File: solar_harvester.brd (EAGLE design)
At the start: 46 x 25.4 mm, 35 parts, among them U1 BQ25505, U2 TPS61322XA, U3 TPS61322XA, U4 MAX17040, U5 INA226

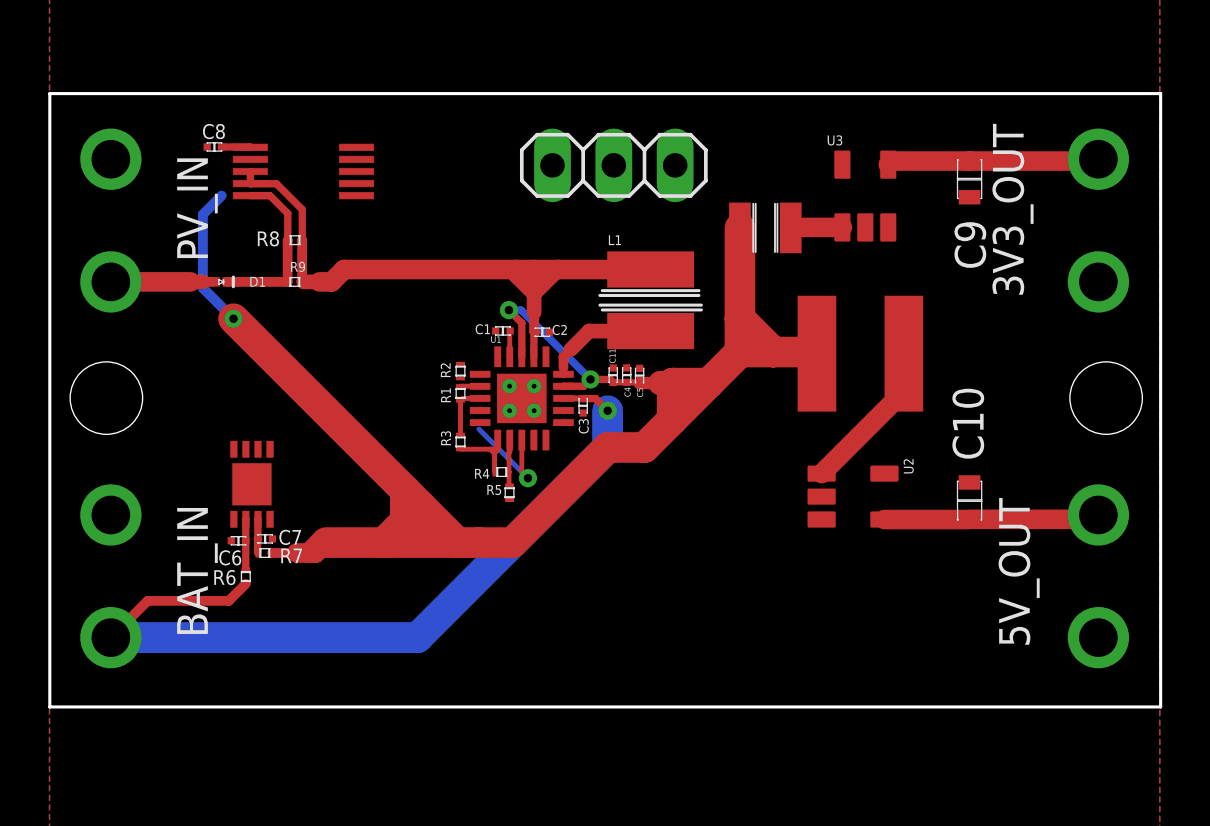
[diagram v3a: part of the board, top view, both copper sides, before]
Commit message: Routing done, without uv protection
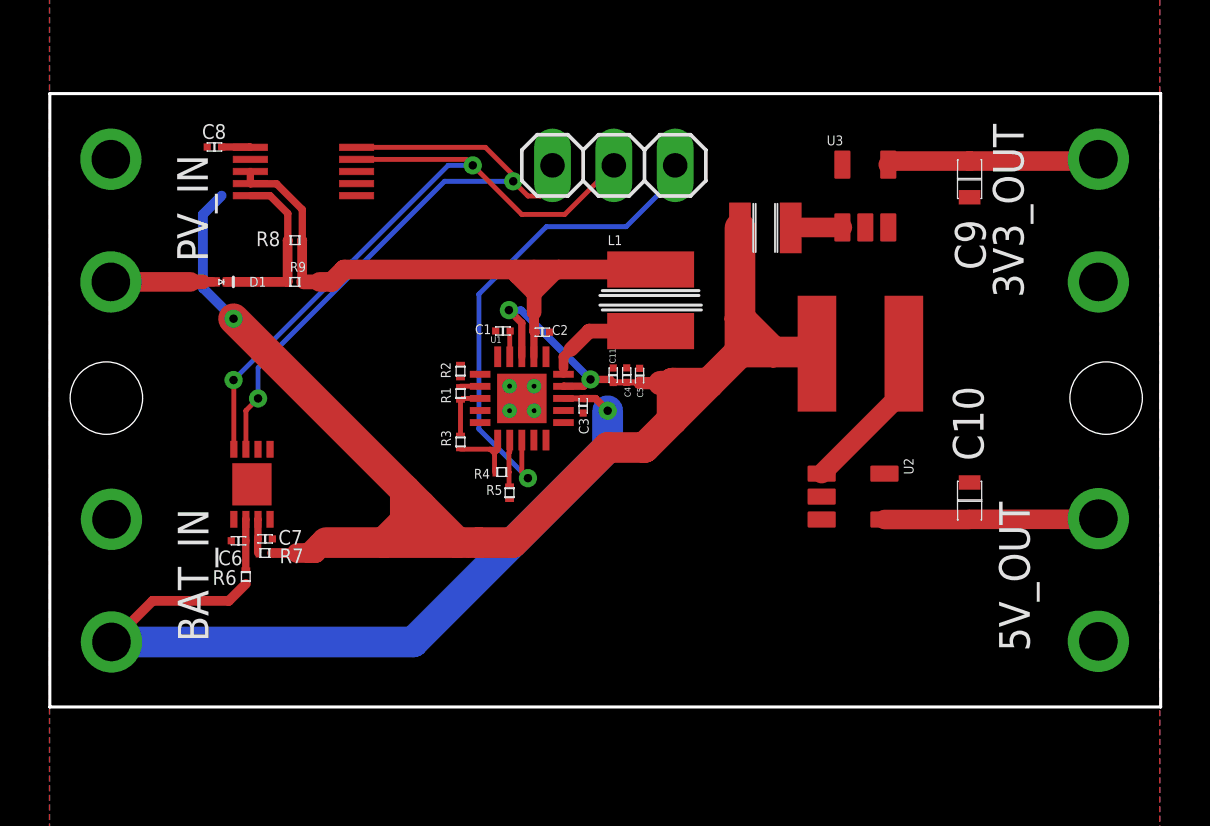
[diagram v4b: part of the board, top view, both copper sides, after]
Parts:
- moved BAT_IN 0.18 mm to (2.57, 10.2)
- moved 5V_OUT 0.15 mm to (43.4, 10.3)
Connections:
- net I2C_SCL: now also JP1.1; no longer JP1.3
- net VBAT_OK: now also JP1.3; no longer JP1.1
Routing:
- net I2C_SDA: track 0.00 -> 28.9 mm, vias 0 -> 2
- net I2C_SCL: track 0.00 -> 27.4 mm, vias 0 -> 2
- net VBAT_OK: track 4.56 -> 20.8 mm
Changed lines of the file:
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@@
 <elements>
 <element name="B1" library="vrlib_board" package="SOLAR_HARVESTER_M1_FOOTPRINT" value="SOLAR_HARVESTER_M1_BOARD" x="23.0124" y="17.7038" smashed="yes" rot="R90"/>
-<element name="BAT_IN" library="vrlib_connector" package="CONN_SCREW_TYPE_2P" value="CONN_SCEW_TYPE_2P" x="2.54" y="10.414" smashed="yes" rot="R90">
-<attribute name="NAME" x="5.286" y="13.398" size="1.27" layer="25" rot="R270"/>
+<element name="BAT_IN" library="vrlib_connector" package="CONN_SCREW_TYPE_2P" value="CONN_SCEW_TYPE_2P" x="2.5654" y="10.2362" smashed="yes" rot="R90">
+<attribute name="NAME" x="5.3114" y="13.2202" size="1.27" layer="25" rot="R270"/>
 </element>
 <element name="C1" library="vrlib_caps" package="0603_FOOTPRINT" value="0.01u" x="18.776" y="20.574" smashed="yes" rot="R270">
@@
 <attribute name="NAME" x="39.068" y="29.146" size="1.27" layer="25" rot="R270"/>
 </element>
-<element name="5V_OUT" library="vrlib_connector" package="CONN_SCREW_TYPE_2P" value="CONN_SCEW_TYPE_2P" x="43.434" y="10.414" smashed="yes" rot="R270">
-<attribute name="NAME" x="39.322" y="13.652" size="1.27" layer="25" rot="R270"/>
+<element name="5V_OUT" library="vrlib_connector" package="CONN_SCREW_TYPE_2P" value="CONN_SCEW_TYPE_2P" x="43.434" y="10.2616" smashed="yes" rot="R270">
+<attribute name="NAME" x="39.322" y="13.4996" size="1.27" layer="25" rot="R270"/>
 </element>
 <element name="PV_IN" library="vrlib_connector" package="CONN_SCREW_TYPE_2P" value="CONN_SCEW_TYPE_2P" x="2.54" y="25.146" smashed="yes" rot="R90">
@@
 <wire x1="21.283" y1="17.78" x2="22.0924" y2="17.78" width="0.254" layer="1"/>
 <wire x1="22.0924" y1="17.78" x2="22.098" y2="17.7744" width="0.254" layer="1"/>
-<wire x1="2.54" y1="7.874" x2="15.24" y2="7.874" width="1.27" layer="16"/>
-<wire x1="15.24" y1="7.874" x2="23.114" y2="15.748" width="1.27" layer="16"/>
+<wire x1="2.5654" y1="7.6962" x2="15.0622" y2="7.6962" width="1.27" layer="16"/>
+<wire x1="15.0622" y1="7.6962" x2="23.114" y2="15.748" width="1.27" layer="16"/>
 <wire x1="23.114" y1="15.748" x2="23.114" y2="17.272" width="1.27" layer="16"/>
 <via x="23.114" y="17.272" extent="1-16" drill="0.35"/>
@@
 <wire x1="22.6116" y1="17.7744" x2="23.114" y2="17.272" width="0.3048" layer="1"/>
 <contactref element="R6" pad="1"/>
-<wire x1="2.54" y1="7.874" x2="4.064" y2="9.398" width="0.4064" layer="1"/>
+<wire x1="2.5654" y1="7.6962" x2="4.2672" y2="9.398" width="0.4064" layer="1"/>
 <wire x1="7.4248" y1="9.398" x2="8.128" y2="10.1012" width="0.4064" layer="1"/>
-<wire x1="4.064" y1="9.398" x2="7.4248" y2="9.398" width="0.4064" layer="1"/>
+<wire x1="4.2672" y1="9.398" x2="7.4248" y2="9.398" width="0.4064" layer="1"/>
 </signal>
 <signal name="N$3">
@@
 <signal name="VBAT_OK">
 <contactref element="U1" pad="13"/>
-<contactref element="JP1" pad="1"/>
 <wire x1="19.558" y1="14.732" x2="19.812" y2="14.478" width="0.2032" layer="1"/>
 <via x="19.812" y="14.478" extent="1-16" drill="0.35"/>
 <wire x1="19.812" y1="14.478" x2="17.78" y2="16.51" width="0.2032" layer="16"/>
 <wire x1="19.558" y1="16.055" x2="19.558" y2="14.732" width="0.2032" layer="1"/>
-<wire x1="17.78" y1="16.51" x2="20.828" y2="27.432" width="0" layer="19" extent="16-16"/>
+<wire x1="17.78" y1="16.51" x2="17.78" y2="22.098" width="0.2032" layer="16"/>
+<wire x1="17.78" y1="22.098" x2="20.574" y2="24.892" width="0.2032" layer="16"/>
+<contactref element="JP1" pad="3"/>
+<wire x1="20.574" y1="24.892" x2="23.876" y2="24.892" width="0.2032" layer="16"/>
+<wire x1="23.876" y1="24.892" x2="25.908" y2="26.924" width="0.2032" layer="16"/>
+<wire x1="25.908" y1="26.924" x2="25.908" y2="27.432" width="0.2032" layer="16"/>
 </signal>
 <signal name="VDD5">
@@
 <wire x1="34.574" y1="12.766" x2="38.066" y2="12.766" width="0.8128" layer="1"/>
 <wire x1="43.2292" y1="12.7746" x2="38.1254" y2="12.7746" width="0.8128" layer="1"/>
-<wire x1="43.2292" y1="12.7746" x2="43.434" y2="12.954" width="0" layer="19" extent="1-1"/>
+<wire x1="43.2292" y1="12.7746" x2="43.434" y2="12.8016" width="0" layer="19" extent="1-1"/>
 <wire x1="38.1" y1="12.8" x2="38.1254" y2="12.7746" width="0" layer="19" extent="1-1"/>
 <wire x1="38.066" y1="12.766" x2="38.1" y2="12.8" width="0" layer="19" extent="1-1"/>
@@
 <contactref element="U4" pad="8"/>
 <contactref element="U5" pad="4"/>
-<wire x1="12.7156" y1="27.678" x2="23.368" y2="27.432" width="0" layer="19" extent="1-1"/>
-<wire x1="7.632" y1="15.674" x2="12.7156" y2="27.678" width="0" layer="19" extent="1-1"/>
+<wire x1="12.7156" y1="27.678" x2="17.28" y2="27.678" width="0.2032" layer="1"/>
+<wire x1="17.28" y1="27.678" x2="17.526" y2="27.432" width="0.2032" layer="1"/>
+<wire x1="17.526" y1="27.432" x2="19.558" y2="25.4" width="0.2032" layer="1"/>
+<wire x1="19.558" y1="25.4" x2="21.336" y2="25.4" width="0.2032" layer="1"/>
+<wire x1="21.336" y1="25.4" x2="23.368" y2="27.432" width="0.2032" layer="1"/>
+<wire x1="7.632" y1="15.674" x2="7.632" y2="18.53" width="0.2032" layer="1"/>
+<wire x1="7.632" y1="18.53" x2="7.62" y2="18.542" width="0.2032" layer="1"/>
+<via x="7.62" y="18.542" extent="1-16" drill="0.35"/>
+<wire x1="7.62" y1="18.542" x2="16.51" y2="27.432" width="0.2032" layer="16"/>
+<wire x1="16.51" y1="27.432" x2="17.526" y2="27.432" width="0.2032" layer="16"/>
+<via x="17.526" y="27.432" extent="1-16" drill="0.35"/>
 </signal>
 <signal name="I2C_SCL">
-<contactref element="JP1" pad="3"/>
 <contactref element="U4" pad="7"/>
 <contactref element="U5" pad="5"/>
-<wire x1="12.7156" y1="28.178" x2="25.908" y2="27.432" width="0" layer="19" extent="1-1"/>
-<wire x1="8.132" y1="15.674" x2="12.7156" y2="28.178" width="0" layer="19" extent="1-1"/>
+<contactref element="JP1" pad="1"/>
+<wire x1="12.7156" y1="28.178" x2="18.05" y2="28.178" width="0.2032" layer="1"/>
+<wire x1="20.828" y1="26.67" x2="20.828" y2="27.432" width="0.2032" layer="1"/>
+<wire x1="20.32" y1="26.162" x2="20.828" y2="26.67" width="0.2032" layer="1"/>
+<wire x1="8.132" y1="15.674" x2="8.132" y2="17.276" width="0.2032" layer="1"/>
+<wire x1="8.132" y1="17.276" x2="8.636" y2="17.78" width="0.2032" layer="1"/>
+<via x="8.636" y="17.78" extent="1-16" drill="0.35"/>
+<wire x1="8.636" y1="17.78" x2="8.636" y2="19.05" width="0.2032" layer="16"/>
+<wire x1="16.3576" y1="26.7716" x2="19.2024" y2="26.7716" width="0.2032" layer="16"/>
+<via x="19.2024" y="26.7716" extent="1-16" drill="0.35"/>
+<wire x1="8.636" y1="19.05" x2="16.3576" y2="26.7716" width="0.2032" layer="16"/>
+<wire x1="18.05" y1="28.178" x2="19.2024" y2="27.0256" width="0.2032" layer="1"/>
+<wire x1="19.2024" y1="27.0256" x2="19.2024" y2="26.7716" width="0.2032" layer="1"/>
+<wire x1="19.2024" y1="26.7716" x2="19.812" y2="26.162" width="0.2032" layer="1"/>
+<wire x1="19.812" y1="26.162" x2="20.32" y2="26.162" width="0.2032" layer="1"/>
 </signal>
 <signal name="N$9">

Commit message: uv added schematic
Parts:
- added U6: DMP3085LSD, vrlib_transistor:SO-8
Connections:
- new net !VB_SEC_ON!: U1.9, U6.2, U6.4
- new net N$15: U6.1, U6.3
- new net VCC_P: C11.1, C4.1, C5.1, U1.19, U1.3, U6.5, U6.6
- net VCC: now also U6.7, U6.8; no longer C11.1, C4.1, C5.1, U1.19, U1.3
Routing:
- net VCC: track 72.8 -> 62.7 mm, vias 3 -> 1
- net VCC_P: track 0.00 -> 10.1 mm, vias 0 -> 2
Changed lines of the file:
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@@
 <attribute name="NAME" x="23.811" y="18.2538" size="0.254" layer="25" rot="R270"/>
+</element>
+<element name="U6" library="vrlib_transistor" package="SO-8" value="DMP3085LSD" x="-4.826" y="5.588" smashed="yes">
+<attribute name="MOUNT" value="SMD" x="-4.826" y="5.588" size="1.778" layer="27" display="off"/>
+<attribute name="NAME" x="-7.493" y="9.525" size="1.27" layer="25"/>
+<attribute name="PACKAGE" value="SO-8" x="-4.826" y="5.588" size="1.778" layer="27" display="off"/>
+<attribute name="VALUE" x="-7.62" y="0.508" size="1.27" layer="27"/>
 </element>
 </elements>
@@
 </signal>
 <signal name="VCC">
-<contactref element="C5" pad="1"/>
 <contactref element="L2" pad="1"/>
 <contactref element="L3" pad="1"/>
-<contactref element="C4" pad="1"/>
-<contactref element="C11" pad="1"/>
-<contactref element="U1" pad="19"/>
-<contactref element="U1" pad="3"/>
-<wire x1="23.3426" y1="18.442" x2="23.3458" y2="18.4452" width="0.254" layer="1"/>
-<wire x1="23.3458" y1="18.4452" x2="23.9014" y2="18.4452" width="0.254" layer="1"/>
-<wire x1="23.9014" y1="18.4452" x2="24.4164" y2="18.4452" width="0.254" layer="1"/>
-<wire x1="24.4164" y1="18.4452" x2="24.4348" y2="18.4268" width="0.254" layer="1"/>
 <wire x1="25.2984" y1="18.415" x2="25.8064" y2="18.415" width="1.016" layer="1"/>
 <wire x1="25.2984" y1="18.415" x2="24.4466" y2="18.415" width="0.508" layer="1"/>
-<wire x1="24.4466" y1="18.415" x2="24.4348" y2="18.4268" width="0.508" layer="1"/>
 <wire x1="27.305" y1="18.415" x2="25.8064" y2="18.415" width="1.27" layer="1"/>
 <wire x1="28.5918" y1="19.7018" x2="27.305" y2="18.415" width="1.27" layer="1"/>
@@
 <contactref element="U5" pad="6"/>
 <contactref element="C8" pad="1"/>
-<via x="22.4028" y="18.5674" extent="1-16" drill="0.35"/>
-<wire x1="21.283" y1="18.28" x2="21.291" y2="18.288" width="0.3048" layer="1"/>
-<wire x1="22.1234" y1="18.288" x2="22.4028" y2="18.5674" width="0.3048" layer="1"/>
-<wire x1="21.291" y1="18.288" x2="22.1234" y2="18.288" width="0.3048" layer="1"/>
-<wire x1="22.4028" y1="18.5674" x2="23.2172" y2="18.5674" width="0.3048" layer="1"/>
-<wire x1="23.2172" y1="18.5674" x2="23.3426" y2="18.442" width="0.3048" layer="1"/>
-<wire x1="22.4028" y1="18.5674" x2="19.5326" y2="21.4376" width="0.3048" layer="16"/>
-<wire x1="19.5326" y1="21.4376" x2="19.0246" y2="21.4376" width="0.3048" layer="16"/>
-<via x="19.0246" y="21.4376" extent="1-16" drill="0.35"/>
-<wire x1="19.0246" y1="21.4376" x2="19.558" y2="20.9042" width="0.3048" layer="1"/>
-<wire x1="19.558" y1="20.9042" x2="19.558" y2="19.505" width="0.3048" layer="1"/>
 <wire x1="27.305" y1="18.415" x2="25.781" y2="16.891" width="1.27" layer="1"/>
 <wire x1="25.781" y1="16.891" x2="24.638" y2="15.748" width="1.27" layer="1"/>
@@
 <wire x1="11.4554" y1="11.811" x2="11.1506" y2="11.811" width="0.8128" layer="1"/>
 <wire x1="11.1506" y1="11.811" x2="10.7188" y2="11.3792" width="0.8128" layer="1"/>
+<contactref element="U6" pad="8"/>
+<contactref element="U6" pad="7"/>
 <wire x1="7.129" y1="26.179" x2="7.129" y2="28.194" width="0" layer="19" extent="1-16"/>
+<wire x1="-5.461" y1="8.288" x2="9.2184" y2="11.3792" width="0" layer="19" extent="1-1"/>
+<wire x1="-6.731" y1="8.288" x2="-5.461" y2="8.288" width="0" layer="19" extent="1-1"/>
 </signal>
 <signal name="N$12">
 </signal>
+<signal name="VCC_P">
+<contactref element="U6" pad="6"/>
+<contactref element="U6" pad="5"/>
+<contactref element="C5" pad="1"/>
+<contactref element="C4" pad="1"/>
+<contactref element="C11" pad="1"/>
+<contactref element="U1" pad="19"/>
+<contactref element="U1" pad="3"/>
+<wire x1="23.3426" y1="18.442" x2="23.3458" y2="18.4452" width="0.254" layer="1"/>
+<wire x1="23.3458" y1="18.4452" x2="23.9014" y2="18.4452" width="0.254" layer="1"/>
+<wire x1="23.9014" y1="18.4452" x2="24.4164" y2="18.4452" width="0.254" layer="1"/>
+<wire x1="24.4164" y1="18.4452" x2="24.4348" y2="18.4268" width="0.254" layer="1"/>
+<via x="22.4028" y="18.5674" extent="1-16" drill="0.35"/>
+<wire x1="21.283" y1="18.28" x2="21.291" y2="18.288" width="0.3048" layer="1"/>
+<wire x1="22.1234" y1="18.288" x2="22.4028" y2="18.5674" width="0.3048" layer="1"/>
+<wire x1="21.291" y1="18.288" x2="22.1234" y2="18.288" width="0.3048" layer="1"/>
+<wire x1="22.4028" y1="18.5674" x2="23.2172" y2="18.5674" width="0.3048" layer="1"/>
+<wire x1="23.2172" y1="18.5674" x2="23.3426" y2="18.442" width="0.3048" layer="1"/>
+<wire x1="22.4028" y1="18.5674" x2="19.5326" y2="21.4376" width="0.3048" layer="16"/>
+<wire x1="19.5326" y1="21.4376" x2="19.0246" y2="21.4376" width="0.3048" layer="16"/>
+<via x="19.0246" y="21.4376" extent="1-16" drill="0.35"/>
+<wire x1="19.0246" y1="21.4376" x2="19.558" y2="20.9042" width="0.3048" layer="1"/>
+<wire x1="19.558" y1="20.9042" x2="19.558" y2="19.505" width="0.3048" layer="1"/>
+<wire x1="-2.921" y1="8.288" x2="19.558" y2="19.505" width="0" layer="19" extent="1-1"/>
+<wire x1="-4.191" y1="8.288" x2="-2.921" y2="8.288" width="0" layer="19" extent="1-1"/>
+</signal>
+<signal name="N$15">
+<contactref element="U6" pad="3"/>
+<contactref element="U6" pad="1"/>
+<wire x1="-4.191" y1="2.888" x2="-6.731" y2="2.888" width="0" layer="19" extent="1-1"/>
+</signal>
+<signal name="!VB_SEC_ON!">
+<contactref element="U1" pad="9"/>
+<contactref element="U6" pad="2"/>
+<contactref element="U6" pad="4"/>
+<wire x1="-2.921" y1="2.888" x2="17.833" y2="17.28" width="0" layer="19" extent="1-1"/>
+<wire x1="-5.461" y1="2.888" x2="-2.921" y2="2.888" width="0" layer="19" extent="1-1"/>
+</signal>
 </signals>

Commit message: uv routed done
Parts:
- moved U6 33.1 mm to (27.4, 13.1)
- moved R1 1.27 mm to (15.7, 18.0)
- moved R2 1.27 mm to (15.7, 18.9)
- moved R3 1.27 mm to (15.7, 16.0)
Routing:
- net !VB_SEC_ON!: track 0.00 -> 26.0 mm, vias 0 -> 2
- net VCC_P: track 10.1 -> 17.9 mm, vias 2 -> 4
- net N$15: track 0.00 -> 4.47 mm
- net N$5: track 3.19 -> 4.46 mm
- net N$4: track 0.82 -> 2.09 mm
- net N$3: track 2.26 -> 3.53 mm
